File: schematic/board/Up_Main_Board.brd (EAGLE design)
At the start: 79.9 x 73.5 mm, 18 parts

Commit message: поправил контур всех плат
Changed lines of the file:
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@@
 <wire x1="13.06603125" y1="57.04941875" x2="14.48953125" y2="62.362009375" width="0.001" layer="20"/>
 <wire x1="31.55733125" y1="14.94365" x2="10.0594" y2="52.179140625" width="0.001" layer="20"/>
-<wire x1="79.71443125" y1="76.777840625" x2="75.794009375" y2="75.35091875" width="0.001" layer="20"/>
+<wire x1="79.71443125" y1="76.777840625" x2="75.794" y2="75.3509" width="0.001" layer="20"/>
 <wire x1="28.86165" y1="83.5" x2="29.5133" y2="79.80428125" width="0.001" layer="20"/>
 <wire x1="40.94246875" y1="14.98626875" x2="41.66693125" y2="10.87763125" width="0.001" layer="20"/>
 <wire x1="65.56791875" y1="17.355859375" x2="68.44266875" y2="14.94365" width="0.001" layer="20"/>
 <wire x1="10.74263125" y1="57.67196875" x2="13.06603125" y2="57.04941875" width="0.001" layer="20"/>
-<wire x1="14.48953125" y1="62.362009375" x2="12.166140625" y2="62.984559375" width="0.001" layer="20"/>
+<wire x1="14.48953125" y1="62.362009375" x2="12.1661" y2="62.984" width="0.001" layer="20"/>
 <wire x1="71.13835" y1="83.5" x2="70.4867" y2="79.80428125" width="0.001" layer="20"/>
 <wire x1="58.33306875" y1="10.87763125" x2="59.05753125" y2="14.98626875" width="0.001" layer="20"/>
@@
 <wire x1="89.9406" y1="52.179140625" x2="68.44266875" y2="14.94365" width="0.001" layer="20"/>
 <wire x1="28.86165" y1="83.5" x2="71.13835" y2="83.5" width="0.001" layer="20"/>
-<wire x1="20.28556875" y1="76.777840625" x2="12.166134375" y2="62.9845625" width="0.001" layer="20" curve="23.082126"/>
+<wire x1="20.28556875" y1="76.777840625" x2="12.1661" y2="62.984" width="0.001" layer="20" curve="23.082126"/>
 <wire x1="10.74263125" y1="57.67196875" x2="10.0594" y2="52.179140625" width="0.001" layer="20" curve="7.934868"/>
 <wire x1="41.66693125" y1="10.87763125" x2="58.33306875" y2="10.87763125" width="0.001" layer="20" curve="24.048625"/>
 <wire x1="89.9406" y1="52.179140625" x2="79.71443125" y2="76.777840625" width="0.001" layer="20" curve="38.901385"/>
 <wire x1="40.94246875" y1="14.98626875" x2="34.43208125" y2="17.355859375" width="0.001" layer="20" curve="120.000035"/>
-<wire x1="65.56791875" y1="17.355859375" x2="59.057534375" y2="14.98626875" width="0.001" layer="20" curve="120.000001"/>
-<wire x1="70.4867" y1="79.80428125" x2="75.79400625" y2="75.350921875" width="0.001" layer="20" curve="120.000013"/>
-<wire x1="24.205990625" y1="75.35091875" x2="29.513296875" y2="79.80428125" width="0.001" layer="20" curve="119.999997"/>
+<wire x1="65.56791875" y1="17.355859375" x2="59.05753125" y2="14.98626875" width="0.001" layer="20" curve="120.000001"/>
+<wire x1="70.4867" y1="79.80428125" x2="75.794" y2="75.3509" width="0.001" layer="20" curve="120.000013"/>
+<wire x1="24.205990625" y1="75.35091875" x2="29.5133" y2="79.80428125" width="0.001" layer="20" curve="119.999997"/>
 </plain>
 <attributes>

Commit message: чипи чипи чапа чапа дуби дуби
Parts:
- moved R4 5.39 mm to (31.7, 27.3)
- moved R17 4.12 mm to (16.9, 63.8)
- moved LED8 2.00 mm to (88.3, 54.4)
- moved JP1 1.12 mm to (34.0, 23.5), turned to 180 degrees
- moved R8 0.58 mm to (82.1, 54.6), turned to 90 degrees
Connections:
- removed net APD_FB_VOLT: U$6.8
- removed net APD_PWM: U$6.9
- removed net COMP_DAC: U$8.13
- removed net LASER_COMP: U$6.6
- removed net N$3: U$8.15
- net USIL_ON: now also U$2.6
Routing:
- net V_BAT: track 168.8 -> 127.2 mm
- net GPS_RX: track 79.5 -> 39.6 mm
- net GPS_TX: track 77.2 -> 42.2 mm
- net GND: track 242.2 -> 214.1 mm
- net 1MISO: track 87.2 -> 61.0 mm
- net 5MOSI: track 91.1 -> 65.9 mm, vias 3 -> 2
- net USIL_ON: track 0.36 -> 23.8 mm, vias 0 -> 1
- net 5MISO: track 80.6 -> 61.2 mm, vias 3 -> 1
- net CE_NRF: track 53.3 -> 34.8 mm, vias 1 -> 0
- net 1SCK: track 62.3 -> 45.1 mm
- net 1MOSI: track 55.3 -> 39.0 mm, vias 1 -> 2
- net 4MOSI: track 39.3 -> 24.3 mm
- net 5V: track 63.2 -> 50.2 mm
- net 3V3: track 186.0 -> 178.0 mm, vias 4 -> 3
- net CS_TDC: track 57.9 -> 51.1 mm, vias 2 -> 0
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
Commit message: добавил полигоны на плату и добавил буквы на разъём
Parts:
- removed U$5: GPS, cansat-lib:GPS
- added U$1: GPS_NEO6M, NEON-BLADE-2024:GPS_NEO6M_NEW
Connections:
- net 5V: now also U$1.P$1; no longer U$5.UCC
- net GND: now also U$1.P$4; no longer U$5.GND
- net GPS_RX: now also U$1.P$3; no longer U$5.TX
- net GPS_TX: now also U$1.P$2; no longer U$5.RX
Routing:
- net 5V: track 50.2 -> 43.4 mm, vias 0 -> 1
- net GPS_TX: track 42.2 -> 39.6 mm
- net 1MISO: track 61.0 -> 60.3 mm
- net GND: track 214.1 -> 214.0 mm, vias 1 -> 2
- added copper zone on layer 1, net 3V3
- added copper zone on layer 1, net 5V
- added copper zone on layer 16, net GND
- added copper zone on layer 1, net N$1
- added copper zone on layer 1, net V_BAT
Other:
- board text added: "3V3"
- board text added: "5V"
- board text added: "CE_NRF"
- board text added: "CS_LIS"
- board text added: "CS_LSM"
- board text added: "CS_NRF"
- board text added: "CS_T"
- board text added: "GND"
- board text added: "MISO"
- board text added: "MOSI"
- board text added: "SCK"
- board text added: "SCL"
- board text added: "SDA"
- board text added: "SDIO0"
- board text added: "SDIO1"
- board text added: "SDIO2"
- board text added: "SDIO3"
- board text added: "SD_CK"
- board text added: "SDС.MD"
- board text added: "T_INT"
- board text added: "U_ON"
- board text added: "V_BAT"

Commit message: Перевернул GPS. Теперь надо переразвести
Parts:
- moved R8 10.8 mm to (85.0, 65.0), turned to 195 degrees
- moved DC-DC_3V3 1.00 mm to (81.0, 51.0)
- moved DC-DC_5V 1.00 mm to (36.0, 51.0)
- moved LED8 0.76 mm to (88.0, 55.1), turned to 195 degrees
- flipped U$1 to the bottom
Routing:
- net GND: track 214.0 -> 225.2 mm, vias 2 -> 4
- net 5V: track 43.4 -> 51.1 mm, vias 1 -> 2
- net CS_LIS: track 63.8 -> 56.6 mm
- net CS_LSM: track 44.2 -> 38.4 mm
- net N$10: track 5.50 -> 10.4 mm
- net 3V3: track 178.4 -> 176.1 mm
- net GPS_RX: track 39.5 -> 41.7 mm, vias 1 -> 2
- net V_BAT: track 127.2 -> 128.5 mm, vias 1 -> 3
- net STATE: track 7.50 -> 6.37 mm
- net GPS_TX: vias 1 -> 2
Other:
- board text added: "DBG"
- board text added: "FLIGHT"
- board text added: "OFF"
- board text added: "ON"
- board text added: "PWR"
- board text added: "VBAT"

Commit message: культивировал плату
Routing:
- net GND: track 225.2 -> 210.7 mm, vias 4 -> 2
- net 5V: track 51.1 -> 51.8 mm, vias 2 -> 1
- net 5MOSI: track 65.9 -> 66.6 mm
- net GPS_TX: track 39.6 -> 39.7 mm, vias 2 -> 1
- net GPS_RX: track 41.7 -> 41.6 mm, vias 2 -> 1
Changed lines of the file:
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@@
 <?xml version="1.0" encoding="utf-8"?>
 <!DOCTYPE eagle SYSTEM "eagle.dtd">
-<eagle version="9.4.2">
+<eagle version="9.6.2">
 <drawing>
 <settings>
-<setting alwaysvectorfont="yes"/>
+<setting alwaysvectorfont="no"/>
 <setting verticaltext="up"/>
 </settings>
@@
 <wire x1="21.23" y1="52.95" x2="23.77" y2="52.95" width="0.5" layer="1"/>
 <wire x1="21.23" y1="71.45" x2="23.77" y2="71.45" width="0.5" layer="1"/>
-<wire x1="40" y1="73.004" x2="25.324" y2="73.004" width="0.5" layer="1"/>
+<wire x1="40" y1="73.004" x2="39.2" y2="73.004" width="0.5" layer="1"/>
+<wire x1="39.2" y1="73.004" x2="25.324" y2="73.004" width="0.5" layer="1"/>
 <wire x1="23.77" y1="71.45" x2="25.324" y2="73.004" width="0.5" layer="1"/>
 <wire x1="40.2800875" y1="73.004" x2="40" y2="73.004" width="0.5" layer="1"/>
@@
 <wire x1="21.23" y1="63.5386375" x2="17.102234375" y2="59.410871875" width="0.2" layer="1"/>
 <contactref element="U$1" pad="P$4"/>
-<wire x1="46.16" y1="71" x2="53.92" y2="71.08" width="0.2" layer="16"/>
 <wire x1="40.004" y1="73" x2="40" y2="73.004" width="0.5" layer="1"/>
 <wire x1="44.92" y1="73" x2="44.92" y2="80.35" width="0.5" layer="1"/>
-<wire x1="52" y1="73" x2="44.92" y2="73" width="0.5" layer="1"/>
-<wire x1="52" y1="73" x2="53.92" y2="71.08" width="0.5" layer="1"/>
 <wire x1="64.63" y1="71.45" x2="63.08" y2="73" width="0.5" layer="1"/>
 <wire x1="64.63" y1="71.45" x2="66.23" y2="71.45" width="0.5" layer="1"/>
-<wire x1="46.16" y1="71" x2="55.84" y2="73" width="0.5" layer="16"/>
-<wire x1="55.84" y1="73" x2="63.08" y2="73" width="0.5" layer="1"/>
 <polygon width="0.2" layer="16">
 <vertex x="8" y="89"/>
@@
 <wire x1="68.77" y1="69.979625" x2="77.2848125" y2="61.4648125" width="0.5" layer="16"/>
 <wire x1="77.2848125" y1="61.4648125" x2="78.9848125" y2="61.4648125" width="0.5" layer="16"/>
-<via x="53.92" y="71.08" extent="1-16" drill="0.35"/>
-<via x="55.84" y="73" extent="1-16" drill="0.35"/>
+<wire x1="63.08" y1="73" x2="46.1" y2="73" width="0.5" layer="1"/>
+<wire x1="46.1" y1="73" x2="44.92" y2="73" width="0.5" layer="1"/>
+<wire x1="46.1" y1="73" x2="46.1" y2="71.06" width="0.5" layer="1"/>
+<wire x1="46.1" y1="71.06" x2="46.16" y2="71" width="0.5" layer="1"/>
 </signal>
 <signal name="3V3">
@@
 <contactref element="U$2" pad="30"/>
 <contactref element="U$1" pad="P$2"/>
-<wire x1="48.73" y1="32.5" x2="48.73" y2="36.73" width="0.2" layer="1"/>
-<wire x1="48.73" y1="36.73" x2="50" y2="38" width="0.2" layer="1"/>
-<wire x1="50" y1="38" x2="50" y2="45" width="0.2" layer="1"/>
-<via x="50" y="45" extent="1-16" drill="0.35"/>
-<wire x1="50" y1="45" x2="50" y2="69.73" width="0.2" layer="16"/>
-<wire x1="50" y1="69.73" x2="51.27" y2="71" width="0.2" layer="1"/>
-<via x="50" y="69.73" extent="1-16" drill="0.35"/>
+<via x="50" y="45.5596" extent="1-16" drill="0.35"/>
+<wire x1="48.73" y1="44.592325" x2="49.697275" y2="45.5596" width="0.2" layer="1"/>
+<wire x1="49.697275" y1="45.5596" x2="50" y2="45.5596" width="0.2" layer="1"/>
+<wire x1="50" y1="45.5596" x2="50" y2="69.73" width="0.2" layer="16"/>
+<wire x1="50" y1="69.73" x2="51.27" y2="71" width="0.2" layer="16"/>
+<wire x1="48.73" y1="32.5" x2="48.73" y2="44.592325" width="0.2" layer="1"/>
 </signal>
 <signal name="GPS_RX">
 <contactref element="U$2" pad="31"/>
 <contactref element="U$1" pad="P$3"/>
-<wire x1="51.27" y1="32.5" x2="51.27" y2="37.27" width="0.2" layer="1"/>
-<wire x1="51.27" y1="37.27" x2="52.4" y2="38.4" width="0.2" layer="1"/>
-<wire x1="52.4" y1="38.4" x2="52.4" y2="45" width="0.2" layer="1"/>
-<via x="52.4" y="45" extent="1-16" drill="0.35"/>
-<wire x1="48.73" y1="71" x2="52.432" y2="69.838" width="0.2" layer="1"/>
-<wire x1="52.432" y1="45.032" x2="52.4" y2="45" width="0.2" layer="16"/>
-<wire x1="52.432" y1="69.838" x2="52.432" y2="45.032" width="0.2" layer="16"/>
-<via x="52.432" y="69.838" extent="1-16" drill="0.35"/>
+<wire x1="51.27" y1="32.5" x2="50.33" y2="33.44" width="0.2" layer="1"/>
+<wire x1="50.33" y1="43.9732" x2="49.7" y2="44.6032" width="0.2" layer="1"/>
+<via x="49.7" y="44.6032" extent="1-16" drill="0.35"/>
+<wire x1="49.7" y1="44.6032" x2="47.9968" y2="44.6032" width="0.2" layer="16"/>
+<wire x1="47.5" y1="69.77" x2="48.73" y2="71" width="0.2" layer="16"/>
+<wire x1="50.33" y1="33.44" x2="50.33" y2="43.9732" width="0.2" layer="1"/>
+<wire x1="47.9968" y1="44.6032" x2="47.5" y2="45.1" width="0.2" layer="16"/>
+<wire x1="47.5" y1="45.1" x2="47.5" y2="69.77" width="0.2" layer="16"/>
 </signal>
 <signal name="SDA">
@@
 <wire x1="48.09" y1="29.3" x2="46.19" y2="31.2" width="0.2" layer="1"/>
 <wire x1="46.19" y1="32.5" x2="46.19" y2="31.2" width="0.2" layer="1"/>
-<wire x1="57.412" y1="31.2981" x2="57.412" y2="37.588" width="0.2" layer="1"/>
-<wire x1="57.412" y1="37.588" x2="57" y2="38" width="0.2" layer="1"/>
 <wire x1="55.4139" y1="29.3" x2="57.412" y2="31.2981" width="0.2" layer="1"/>
 <wire x1="48.09" y1="29.3" x2="55.4139" y2="29.3" width="0.2" layer="1"/>
 <via x="57.5" y="50.9" extent="1-16" drill="0.35"/>
-<wire x1="57" y1="38" x2="57" y2="45.8861" width="0.2" layer="1"/>
-<wire x1="57" y1="45.8861" x2="57.412" y2="46.2981" width="0.2" layer="1"/>
+<wire x1="57.412" y1="31.2981" x2="57.412" y2="50.812" width="0.2" layer="1"/>
 <wire x1="57.412" y1="50.812" x2="57.5" y2="50.9" width="0.2" layer="1"/>
-<wire x1="57.412" y1="46.2981" x2="57.412" y2="50.812" width="0.2" layer="1"/>
 <wire x1="57.5" y1="50.9" x2="57.5" y2="76.5" width="0.2" layer="16"/>
 <wire x1="57.5" y1="76.5" x2="58" y2="77" width="0.2" layer="16"/>
@@
 <wire x1="54.3" y1="29.3" x2="55" y2="30" width="0.2" layer="16"/>
 <via x="55" y="30" extent="1-16" drill="0.35"/>
-<wire x1="55" y1="30" x2="55" y2="49" width="0.2" layer="1"/>
-<via x="55" y="49" extent="1-16" drill="0.35"/>
-<wire x1="55" y1="49" x2="55" y2="80.27" width="0.2" layer="16"/>
-<wire x1="55" y1="80.27" x2="55.08" y2="80.35" width="0.2" layer="16"/>
+<wire x1="55.2" y1="30.2" x2="55" y2="30" width="0.2" layer="1"/>
+<via x="55.2" y="50.8" extent="1-16" drill="0.35"/>
+<wire x1="55.08" y1="80.35" x2="55.2" y2="80.23" width="0.2" layer="16"/>
+<wire x1="55.2" y1="80.23" x2="55.2" y2="50.8" width="0.2" layer="16"/>
 <wire x1="44.31" y1="29.3" x2="54.3" y2="29.3" width="0.2" layer="16"/>
+<wire x1="55.9" y1="34.3139" x2="55.2" y2="33.6139" width="0.2" layer="1"/>
+<wire x1="55.2" y1="50.8" x2="55.2" y2="46.3861" width="0.2" layer="1"/>
+<wire x1="55.2" y1="46.3861" x2="55.9" y2="45.6861" width="0.2" layer="1"/>
+<wire x1="55.9" y1="45.6861" x2="55.9" y2="34.3139" width="0.2" layer="1"/>
+<wire x1="55.2" y1="33.6139" x2="55.2" y2="30.2" width="0.2" layer="1"/>
 </signal>
 <signal name="SDIO_CK">
@@
 <polygon width="0.2" layer="1">
 <vertex x="30" y="72"/>
-<vertex x="47.1" y="72"/>
-<vertex x="47.1" y="70.1"/>
-<vertex x="44" y="67"/>
+<vertex x="56" y="72"/>
+<vertex x="56" y="67"/>
 <vertex x="29" y="67"/>
 <vertex x="12" y="50"/>
@@
 <wire x1="31.23" y1="71.45" x2="33.77" y2="71.45" width="0.5" layer="1"/>
 <wire x1="33.77" y1="71.45" x2="36.724" y2="68.496" width="0.5" layer="1"/>
-<wire x1="43.656" y1="68.496" x2="53.84" y2="71" width="0.5" layer="16"/>
-<wire x1="36.724" y1="68.496" x2="43.656" y2="68.496" width="0.5" layer="1"/>
-<via x="43.656" y="68.496" extent="1-16" drill="0.35"/>
+<wire x1="51.336" y1="68.496" x2="53.84" y2="71" width="0.5" layer="1"/>
+<wire x1="36.724" y1="68.496" x2="51.336" y2="68.496" width="0.5" layer="1"/>
 </signal>
 <signal name="V_BAT">

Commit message: забыли моторчик...
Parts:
- removed JP1, JP4: (no value), pinhead:1X02
- added R1, R2: 10k, rcl:R0603
- added R3, R5: 100, rcl:R0603
- added U$3: IRF7905PBF, NEON-BLADE-2024:SO8
- added X1, X2, X3, X4: JST-2-K-S, NEON-BLADE-2024:B2B-PH-K-S
- moved R4 4.03 mm to (28.0, 28.9), turned to 180 degrees
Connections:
- removed net N$37: JP1.2, R4.2
- new net DRUGATEL: R5.1, U$2.3
- new net N$2: U$3.5, U$3.6, X3.1
- new net N$3: R2.1, R5.2, U$3.4
- new net N$5: R1.2, R3.2, U$3.2
- new net N$6: R4.2, X2.2
- new net N$8: U$3.7, U$3.8, X4.1
- new net PERESHIGATEL: R3.1, U$2.21
- net 3V3: now also X2.1; no longer JP1.1
- net 5V: now also X3.2
- net CS_LIS: now also U$2.10; no longer U$2.3
- net GND: now also R1.1, R2.2, U$3.1, U$3.3, X1.2; no longer JP4.2
- net N$1: now also X1.1, X4.2; no longer JP4.1
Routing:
- net 5V: track 51.8 -> 113.1 mm
- net GND: track 210.7 -> 249.9 mm, vias 2 -> 7
- net PERESHIGATEL: track 0.00 -> 38.5 mm, vias 0 -> 1
- net N$8: track 0.00 -> 34.9 mm
- net DRUGATEL: track 0.00 -> 28.2 mm, vias 0 -> 1
- net CS_LIS: track 56.6 -> 41.3 mm, vias 0 -> 1
- net N$1: track 4.36 -> 16.5 mm
- net N$2: track 0.00 -> 10.7 mm
- net N$5: track 0.00 -> 9.06 mm
- net N$3: track 0.00 -> 4.61 mm
- net N$6: track 0.00 -> 3.78 mm
- net N$37: track 3.38 -> 0.00 mm
- net 4MISO: track 41.0 -> 43.4 mm, vias 1 -> 3
- net 3V3: track 176.1 -> 174.2 mm
- net 4SCK: track 52.1 -> 53.8 mm, vias 1 -> 3
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- added copper zone on layer 1, net N$8
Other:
- board text added: "G"
- board text added: "LED"
- board text added: "MOTOR"
- board text added: "PEREG"
- board text added: "VB"

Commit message: забыи отладочные пины...
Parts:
- added JP1: (no value), pinhead:1X04/90
- moved R1 0.30 mm to (58.4, 22.0)
- moved R2 0.20 mm to (58.4, 26.7)
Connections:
- removed net TDC_INT: U$6.7
- removed net USIL_ON: U$2.6, U$6.1
- new net APD_FB_VOLT: U$2.9, U$6.8
- new net APD_PWM: U$2.8, U$6.9
- new net DBG_3V3: JP1.4, U$2.3V3
- new net SWC: JP1.2, U$2.SWC
- new net SWD: JP1.3, U$2.SWD
- net GND: now also JP1.1, U$2.GND
- net PHOTORES: now also U$2.36
- net STATE: now also U$2.4
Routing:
- net PHOTORES: track 2.97 -> 81.8 mm, vias 0 -> 2
- net STATE: track 6.37 -> 54.2 mm, vias 0 -> 1
- net SWC: track 0.00 -> 38.8 mm, vias 0 -> 1
- net APD_FB_VOLT: track 0.00 -> 35.2 mm, vias 0 -> 1
- net APD_PWM: track 0.00 -> 34.5 mm, vias 0 -> 1
- net SWD: track 0.00 -> 33.8 mm, vias 0 -> 1
- net DBG_3V3: track 0.00 -> 29.1 mm, vias 0 -> 1
- net USIL_ON: track 22.7 -> 0.00 mm, vias 1 -> 0
- net 5V: track 113.1 -> 125.8 mm, vias 1 -> 3
- net 5MOSI: track 66.6 -> 57.9 mm
- net 5MISO: track 60.9 -> 52.4 mm
- net GND: track 249.9 -> 243.4 mm, vias 7 -> 8
- net 4MOSI: track 24.6 -> 31.0 mm
- net DRUGATEL: track 28.2 -> 31.4 mm, vias 1 -> 2
- net 3V3: track 174.2 -> 177.0 mm
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- added copper zone on layer 1, net GND
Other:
- board text added: "CE_RF"
- board text added: "CS_LM"
- board text added: "CS_RF"
- board text added: "SDСMD"
- board text added: "SWC"
- board text added: "SWD"
- board text removed: "CE_NRF"
- board text removed: "CS_LSM"
- board text removed: "CS_NRF"
- board text removed: "SDС.MD"
- board text removed: "T_INT"
- board text removed: "U_ON"
- board text removed: "V_BAT"

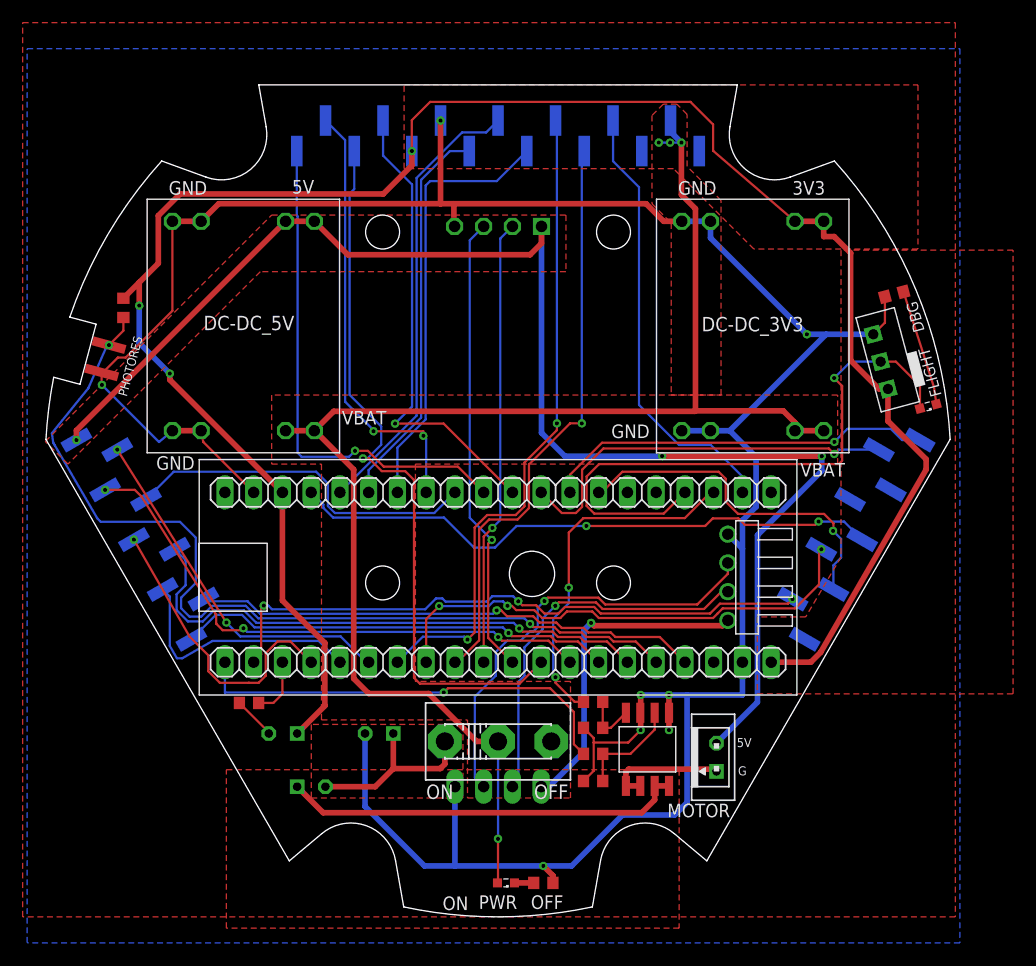
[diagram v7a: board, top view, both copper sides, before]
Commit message: Проверил плату верхнюю. Осталось только убрать у GPS отверстие под антенну, чтобы оно не мешало полигону земли
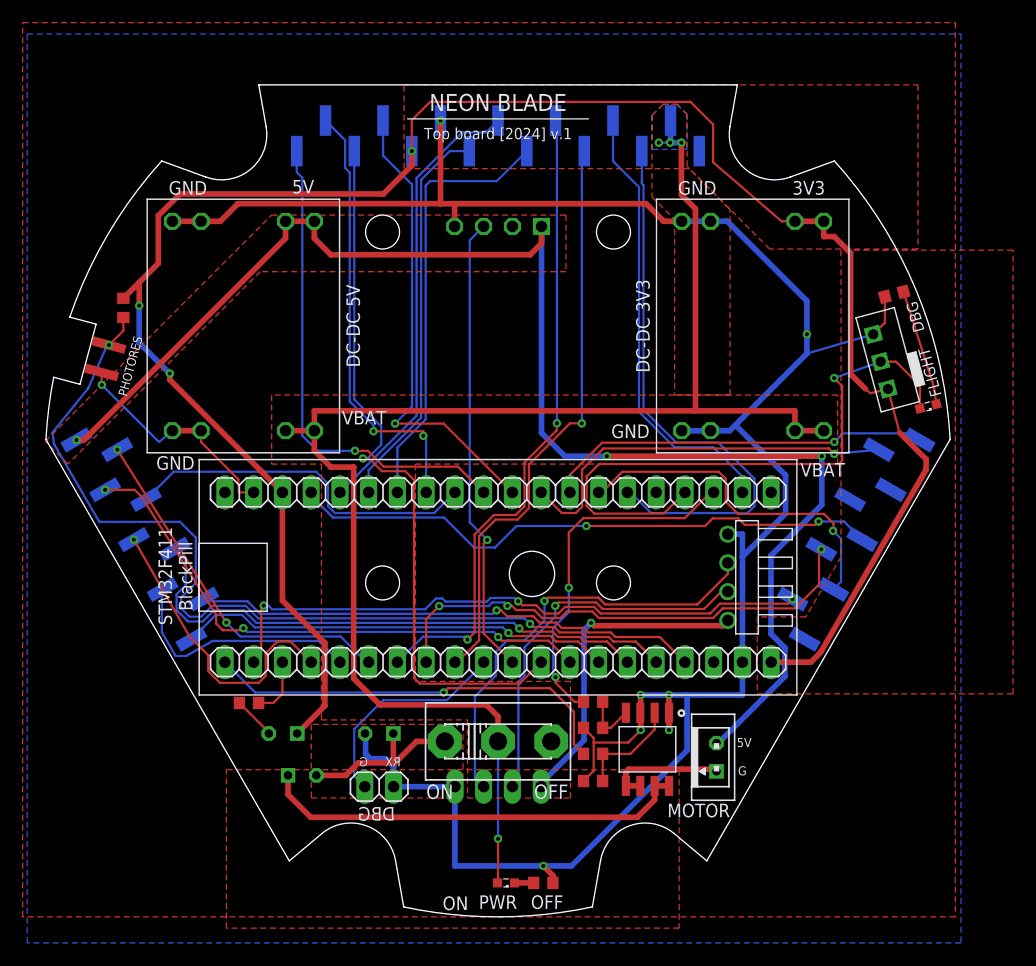
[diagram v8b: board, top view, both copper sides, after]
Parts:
- added JP2: (no value), pinhead:1X02
- moved X4 1.28 mm to (32.7, 22.5)
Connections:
- removed net GPS_TX: U$1.P$2, U$2.30
- new net BUZZER: U$2.6, U$8.13
- new net DBG_TX: JP2.1, U$2.30
- net GND: now also JP2.2
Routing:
- net BUZZER: track 0.00 -> 49.9 mm
- net GPS_TX: track 39.6 -> 0.00 mm, vias 1 -> 0
- net DBG_TX: track 0.00 -> 19.4 mm
- net GND: track 243.4 -> 224.7 mm
- net V_BAT: track 128.9 -> 133.5 mm
- net N$8: track 35.5 -> 38.1 mm
- net 5V: track 125.8 -> 128.2 mm
- net PERESHIGATEL: track 38.6 -> 37.0 mm
- net 1SCK: track 45.0 -> 43.4 mm
- net N$1: track 16.5 -> 15.2 mm
- net 3V3: track 177.0 -> 178.3 mm
- added copper zone on layer 16, net V_BAT
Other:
- board text added: "APD_FB"
- board text added: "APD_PWM"
- board text added: "CS_TDC"
- board text added: "DC-DC 3V3"
- board text added: "DC-DC 5V"
- board text added: "GPS NEO-6M"
- board text added: "NEON BLADE"
- board text added: "RX"
- board text added: "STM32F411 BlackPill"
- board text added: "TX"
- board text added: "Top board [2024] v.1"
- board text added: "[NC]"
- board text removed: "CS_T"
